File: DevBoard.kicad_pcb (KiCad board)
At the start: 2 copper layers, 71 parts, among them J1 Conn_01x06, J10 DB25_Female_MountingHoles, J11 Conn_01x02_Male, J12 3.5mmStereoJack, J13 6.35mmMonoAudioJack, J14 Conn_01x02_Female, J15 6.35mmMonoAudioJack, J16 Conn_01x02_Female, J17 6.35mmMonoAudioJack, J18 Conn_01x02_Female, J19 6.35mmMonoAudioJack, J2 USB_B_Micro, J20 Conn_01x02_Female, J21 6.35mmMonoAudioJack, J22 Conn_01x02_Female, J23 6.35mmMonoAudioJack, J24 Conn_01x02_Female, J25 6.35mmMonoAudioJack, J26 Conn_01x02_Female, J27 6.35mmMonoAudioJack, J28 Conn_01x02_Female, J29 6.35mmMonoAudioJack, J3 Debug Headers, J30 Conn_01x02_Female, J31 6.35mmMonoAudioJack, J32 Conn_01x02_Female, J4 MIDI_TX_Out, J5 KeyboadDin5, J6 KeyboardMiniDin6, J7 Conn_01x08_Female, J8 Conn_01x08_Male, J9 Conn_01x08_Male, SW1 SW_Push, U1 STM32L476RCTx, U2 LD1117S33CTR

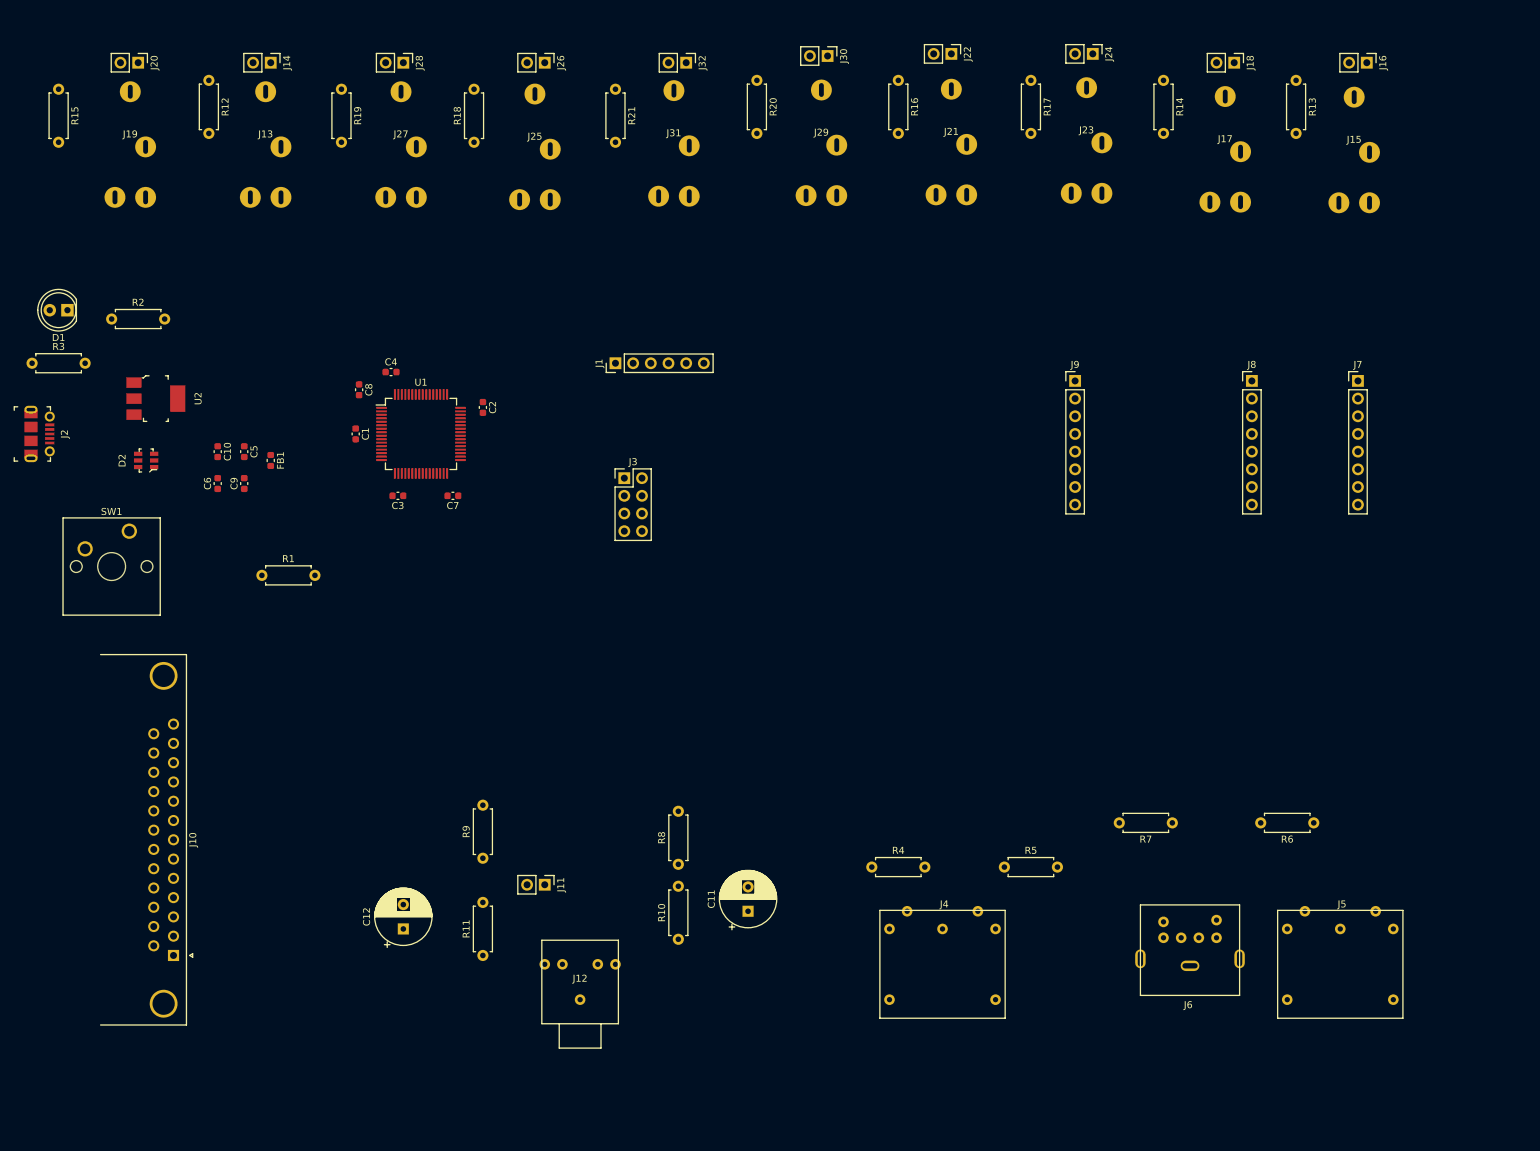
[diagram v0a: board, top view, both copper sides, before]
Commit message: added board layout
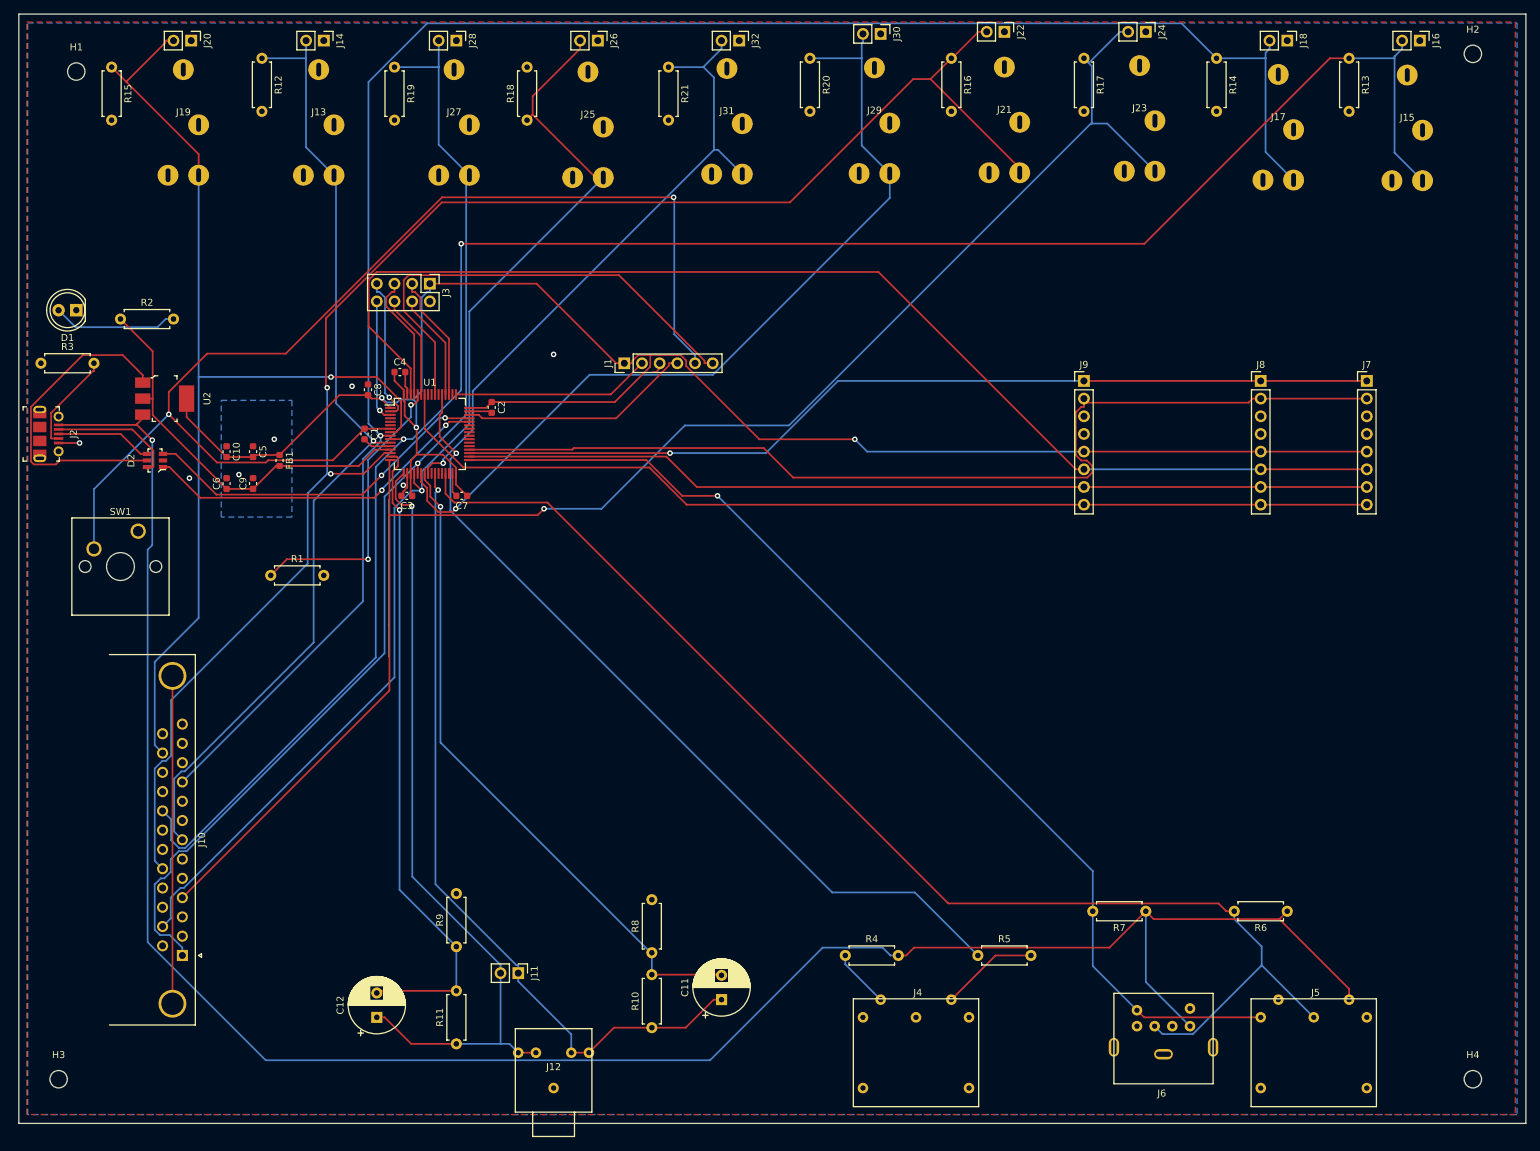
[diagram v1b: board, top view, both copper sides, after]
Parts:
- added H1: MountingHole, MountingHole:MountingHole_2.5mm, F.Cu at (20.3, 20.3)
- added H2: MountingHole, MountingHole:MountingHole_2.5mm, F.Cu at (221.0, 17.8)
- added H3: MountingHole, MountingHole:MountingHole_2.5mm, F.Cu at (17.8, 165.1)
- added H4: MountingHole, MountingHole:MountingHole_2.5mm, F.Cu at (221.0, 165.1)
- moved J3 39.5 mm to (71.1, 50.8), turned to 270 degrees
- moved R8 13.3 mm to (103.0, 146.9)
- moved R10 13.3 mm to (103.0, 157.7)
- moved C12 13.3 mm to (63.5, 156.2)
- moved J11 13.3 mm to (83.8, 149.9)
- moved J6 13.3 mm to (176.5, 159.3)
- moved J12 13.3 mm to (88.9, 163.8)
- moved R11 13.3 mm to (74.9, 160.0)
- moved R9 13.3 mm to (74.9, 146.1)
- moved C11 13.3 mm to (113.0, 153.7)
- moved J4 13.3 mm to (141.0, 161.3)
- moved J5 13.3 mm to (198.1, 161.3)
- moved R4 13.3 mm to (130.8, 147.3)
- moved R6 13.3 mm to (194.3, 141.0)
- moved R7 13.3 mm to (174.0, 141.0)
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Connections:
- C4 pad 1: Net-(C4-Pad1) -> G_3.3
- C7 pad 1: Net-(C7-Pad1) -> G_3.3
- J1 pad 3: Net-(J1-Pad3) -> GND
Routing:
- net G_5V: track 0.00 -> 305.0 mm, vias 0 -> 1
- net /ASignal3: track 0.00 -> 280.5 mm, vias 0 -> 2
- net G_3.3: track 0.00 -> 272.3 mm, vias 0 -> 3
- net /ASignal2: track 0.00 -> 270.9 mm, vias 0 -> 1
- net /Audio/ASignal5: track 0.00 -> 231.2 mm, vias 0 -> 2
- net /Audio/ASignal6: track 0.00 -> 228.8 mm, vias 0 -> 1
- net /Keyboard_DATA: track 0.00 -> 181.0 mm
- net /PS2_CS: track 0.00 -> 174.6 mm
- net /NRST: track 0.00 -> 173.0 mm, vias 0 -> 2
- net /Audio/ASignal7: track 0.00 -> 166.4 mm, vias 0 -> 1
- net /Audio/ASignal8: track 0.00 -> 163.2 mm, vias 0 -> 1
- net /Keyboard_CLK: track 0.00 -> 154.9 mm, vias 0 -> 1
- net /ASignal1: track 0.00 -> 152.3 mm, vias 0 -> 1
- net /PS2_MOSI: track 0.00 -> 145.3 mm
- net /PS2_AWK: track 0.00 -> 144.8 mm
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- added copper zone on B.Cu, net (none)
- added copper zone on B.Cu, net GND
- added copper zone on F.Cu, net GND
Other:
- board outline added: 216.5 x 159.4 mm

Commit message: thing i finished the layout
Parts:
- moved C7 3.76 mm to (79.2, 80.0), turned to 270 degrees
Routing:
- net GND: track 21.4 -> 74.6 mm, vias 7 -> 8
- net (no net): track 22.6 -> 0.00 mm
- net /NRST: track 173.0 -> 175.6 mm
- net G_3.3: track 272.3 -> 274.4 mm
- removed copper zone on B.Cu, net (none)
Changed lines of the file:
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@@
     (thickness 1.6)
     (drawings 4)
-    (tracks 603)
+    (tracks 627)
     (zones 0)
     (modules 75)
@@
   )
   (module Capacitor_SMD:C_0603_1608Metric (layer F.Cu)
-    (at 75.705 81.28 180)
+    (at 79.248 80.023 270)
     (descr "Capacitor SMD 0603 (1608 Metric), square (rectangular) end terminal, IPC_7351 nominal, (Body size source: IPC-SM-782 page 76, https://www.pcb-3d.com/wordpress/wp-content/uploads/ipc-sm-782a_amendment_1_and_2.pdf), generated with kicad-footprint-generator")
     (tags capacitor)
     (attr smd)
-    (fp_text reference C7 (at 0 -1.43) (layer F.SilkS)
+    (fp_text reference C7 (at 0 -1.43 90) (layer F.SilkS)
       (effects (font (size 1 1) (thickness 0.15)))
     )
-    (fp_text value "CAP 0.1 uf" (at 0 1.43) (layer F.Fab)
+    (fp_text value "CAP 0.1 uf" (at 0 1.43 90) (layer F.Fab)
       (effects (font (size 1 1) (thickness 0.15)))
     )
@@
     (fp_line (start -0.8 -0.4) (end 0.8 -0.4) (layer F.Fab) (width 0.1))
     (fp_line (start -0.8 0.4) (end -0.8 -0.4) (layer F.Fab) (width 0.1))
-    (fp_text user %R (at 0 0) (layer F.Fab)
+    (fp_text user %R (at 0 0 90) (layer F.Fab)
       (effects (font (size 0.4 0.4) (thickness 0.06)))
     )
-    (pad 1 smd roundrect (at -0.775 0 180) (size 0.9 0.95) (layers F.Cu F.Paste F.Mask) (roundrect_rratio 0.25)
+    (pad 1 smd roundrect (at -0.775 0 270) (size 0.9 0.95) (layers F.Cu F.Paste F.Mask) (roundrect_rratio 0.25)
       (net 4 G_3.3))
-    (pad 2 smd roundrect (at 0.775 0 180) (size 0.9 0.95) (layers F.Cu F.Paste F.Mask) (roundrect_rratio 0.25)
+    (pad 2 smd roundrect (at 0.775 0 270) (size 0.9 0.95) (layers F.Cu F.Paste F.Mask) (roundrect_rratio 0.25)
       (net 2 GND))
     (model ${KISYS3DMOD}/Capacitor_SMD.3dshapes/C_0603_1608Metric.wrl
@@
   (gr_line (start 12.065 171.45) (end 228.6 171.45) (layer Edge.Cuts) (width 0.05))
   (gr_line (start 12.065 12.065) (end 12.065 171.45) (layer Edge.Cuts) (width 0.05))
-  (segment (start 65.278 104.394) (end 65.278 99.822) (width 0.25) (layer B.Cu) (net 0))
-  (segment (start 65.278 99.822) (end 65.278 81.788) (width 0.25) (layer B.Cu) (net 0))
+  (segment (start 65.278 104.394) (end 65.278 99.822) (width 0.25) (layer B.Cu) (net 2))
+  (segment (start 65.278 99.822) (end 65.278 81.788) (width 0.25) (layer B.Cu) (net 2))
+  (segment (start 67.31 49.784) (end 67.31 60.198) (width 0.25) (layer B.Cu) (net 2))
+  (segment (start 67.31 60.198) (end 65.532 61.976) (width 0.25) (layer B.Cu) (net 2))
+  (segment (start 65.532 61.976) (end 65.532 61.976) (width 0.25) (layer B.Cu) (net 2))
+  (segment (start 67.31 49.784) (end 67.31 46.482) (width 0.25) (layer B.Cu) (net 2))
+  (via (at 65.532 61.976) (size 0.8) (drill 0.4) (layers F.Cu B.Cu) (net 2))
   (segment (start 22.86 62.23) (end 22.86 63.3553) (width 0.25) (layer F.Cu) (net 1))
   (segment (start 22.86 63.3553) (end 22.7193 63.3553) (width 0.25) (layer F.Cu) (net 1))
@@
   (segment (start 16.7118 72.9721) (end 16.7797 73.04) (width 0.25) (layer F.Cu) (net 1))
   (segment (start 16.7797 73.04) (end 17.78 73.04) (width 0.25) (layer F.Cu) (net 1))
-  (segment (start 74.37 78.065) (end 74.37 80.72) (width 0.25) (layer F.Cu) (net 2))
-  (segment (start 74.37 80.72) (end 74.93 81.28) (width 0.25) (layer F.Cu) (net 2))
   (segment (start 67.87 78.065) (end 67.87 80.085) (width 0.25) (layer F.Cu) (net 2))
   (segment (start 67.87 80.085) (end 67.31 80.645) (width 0.25) (layer F.Cu) (net 2))
@@
   (via (at 43.688 78.232) (size 0.8) (drill 0.4) (layers F.Cu B.Cu) (net 2))
   (via (at 67.31 79.756) (size 0.8) (drill 0.4) (layers F.Cu B.Cu) (net 2))
+  (segment (start 66.285702 74.14) (end 67.84501 75.699308) (width 0.25) (layer F.Cu) (net 2))
+  (segment (start 65.445 74.14) (end 66.285702 74.14) (width 0.25) (layer F.Cu) (net 2))
+  (segment (start 67.84501 77.49701) (end 67.84501 76.73501) (width 0.25) (layer F.Cu) (net 2))
+  (segment (start 67.87 77.522) (end 67.84501 77.49701) (width 0.25) (layer F.Cu) (net 2))
+  (segment (start 67.87 78.065) (end 67.87 77.522) (width 0.25) (layer F.Cu) (net 2))
+  (segment (start 67.84501 76.73501) (end 67.84501 77.199308) (width 0.25) (layer F.Cu) (net 2))
+  (segment (start 67.84501 75.699308) (end 67.84501 76.73501) (width 0.25) (layer F.Cu) (net 2))
+  (segment (start 65.532 61.976) (end 66.294 61.976) (width 0.25) (layer F.Cu) (net 2))
+  (segment (start 66.294 61.976) (end 67.564 63.246) (width 0.25) (layer F.Cu) (net 2))
+  (segment (start 65.278 104.394) (end 65.278 104.902) (width 0.25) (layer B.Cu) (net 2))
+  (segment (start 65.278 104.902) (end 65.278 105.41) (width 0.25) (layer B.Cu) (net 2))
+  (segment (start 65.278 81.788) (end 65.786 81.788) (width 0.25) (layer B.Cu) (net 2))
+  (segment (start 65.786 81.788) (end 66.04 81.788) (width 0.25) (layer B.Cu) (net 2))
+  (segment (start 74.37 78.065) (end 74.37 80.212) (width 0.25) (layer F.Cu) (net 2))
+  (segment (start 74.37 80.212) (end 74.93 80.772) (width 0.25) (layer F.Cu) (net 2))
+  (segment (start 74.93 80.772) (end 79.502 80.772) (width 0.25) (layer F.Cu) (net 2))
   (segment (start 33.6112 69.5707) (end 22.86 80.3219) (width 0.25) (layer B.Cu) (net 3))
   (segment (start 22.86 80.3219) (end 22.86 88.9) (width 0.25) (layer B.Cu) (net 3))
-  (segment (start 106.141 38.3902) (end 106.238 38.4867) (width 0.25) (layer B.Cu) (net 3))
-  (segment (start 106.238 38.4867) (end 106.238 58.0727) (width 0.25) (layer B.Cu) (net 3))
   (segment (start 106.238 58.0727) (end 109.22 61.0547) (width 0.25) (layer B.Cu) (net 3))
   (segment (start 109.22 61.0547) (end 109.22 62.23) (width 0.25) (layer B.Cu) (net 3))
-  (segment (start 33.6112 69.5707) (end 33.6112 66.3673) (width 0.25) (layer F.Cu) (net 3))
-  (segment (start 33.6112 66.3673) (end 39.1337 60.8448) (width 0.25) (layer F.Cu) (net 3))
-  (segment (start 39.1337 60.8448) (end 50.4167 60.8448) (width 0.25) (layer F.Cu) (net 3))
-  (segment (start 50.4167 60.8448) (end 72.8713 38.3902) (width 0.25) (layer F.Cu) (net 3))
-  (segment (start 72.8713 38.3902) (end 106.141 38.3902) (width 0.25) (layer F.Cu) (net 3))
   (segment (start 65.445 71.64) (end 61.76 71.64) (width 0.25) (layer F.Cu) (net 3))
   (segment (start 61.76 71.64) (end 61.735 71.615) (width 0.25) (layer F.Cu) (net 3))
@@
   (segment (start 40.5354 76.4949) (end 33.6112 69.5707) (width 0.25) (layer F.Cu) (net 3))
   (via (at 33.6112 69.5707) (size 0.8) (layers F.Cu B.Cu) (net 3))
-  (via (at 106.141 38.3902) (size 0.8) (layers F.Cu B.Cu) (net 3))
+  (segment (start 106.68 39.878) (end 108.204 38.354) (width 0.25) (layer B.Cu) (net 3))
+  (segment (start 106.68 39.878) (end 106.426 40.132) (width 0.25) (layer B.Cu) (net 3))
+  (segment (start 106.426 40.132) (end 106.426 57.94) (width 0.25) (layer B.Cu) (net 3))
+  (segment (start 108.204 38.354) (end 108.204 38.354) (width 0.25) (layer B.Cu) (net 3))
+  (via (at 108.204 38.354) (size 0.8) (drill 0.4) (layers F.Cu B.Cu) (net 3))
+  (segment (start 108.1678 38.3902) (end 108.204 38.354) (width 0.25) (layer F.Cu) (net 3))
+  (segment (start 72.8713 38.3902) (end 108.1678 38.3902) (width 0.25) (layer F.Cu) (net 3))
+  (segment (start 50.4167 60.8448) (end 72.8713 38.3902) (width 0.25) (layer F.Cu) (net 3))
+  (segment (start 39.1337 60.8448) (end 50.4167 60.8448) (width 0.25) (layer F.Cu) (net 3))
+  (segment (start 33.6112 66.3673) (end 39.1337 60.8448) (width 0.25) (layer F.Cu) (net 3))
+  (segment (start 33.6112 69.5707) (end 33.6112 66.3673) (width 0.25) (layer F.Cu) (net 3))
   (segment (start 74.87 78.065) (end 74.87 79.67) (width 0.25) (layer F.Cu) (net 4))
-  (segment (start 74.87 79.67) (end 76.48 81.28) (width 0.25) (layer F.Cu) (net 4))
   (segment (start 69.2284 75.3616) (end 73.0102 75.3616) (width 0.25) (layer F.Cu) (net 4))
   (segment (start 73.0102 75.3616) (end 74.87 77.2214) (width 0.25) (layer F.Cu) (net 4))
@@
   (segment (start 66.04 63.5) (end 66.04 64.749215) (width 0.25) (layer F.Cu) (net 4))
   (segment (start 66.04 64.749215) (end 67.330785 66.04) (width 0.25) (layer F.Cu) (net 4))
+  (segment (start 78.654 79.67) (end 79.08 79.67) (width 0.25) (layer F.Cu) (net 4))
+  (segment (start 74.87 79.67) (end 78.654 79.67) (width 0.25) (layer F.Cu) (net 4))
+  (segment (start 78.654 79.67) (end 78.826 79.67) (width 0.25) (layer F.Cu) (net 4))
   (segment (start 29.87 67.31) (end 31.2953 67.31) (width 0.25) (layer F.Cu) (net 5))
   (segment (start 41.91 80.29) (end 31.2953 69.6753) (width 0.25) (layer F.Cu) (net 5))
@@
       )
     )
-  )
-  (zone (net 0) (net_name "") (layer B.Cu) (hatch edge 0.508)
-    (connect_pads (clearance 0.508))
-    (min_thickness 0.254)
-    (fill yes (arc_segments 32) (thermal_gap 0.508) (thermal_bridge_width 0.508))
-    (polygon
-      (pts
-        (xy 51.308 84.328) (xy 41.148 84.328) (xy 41.148 67.564) (xy 51.308 67.564)
-      )
-    )
